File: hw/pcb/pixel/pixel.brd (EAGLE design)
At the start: 160 x 100 mm, 0 parts

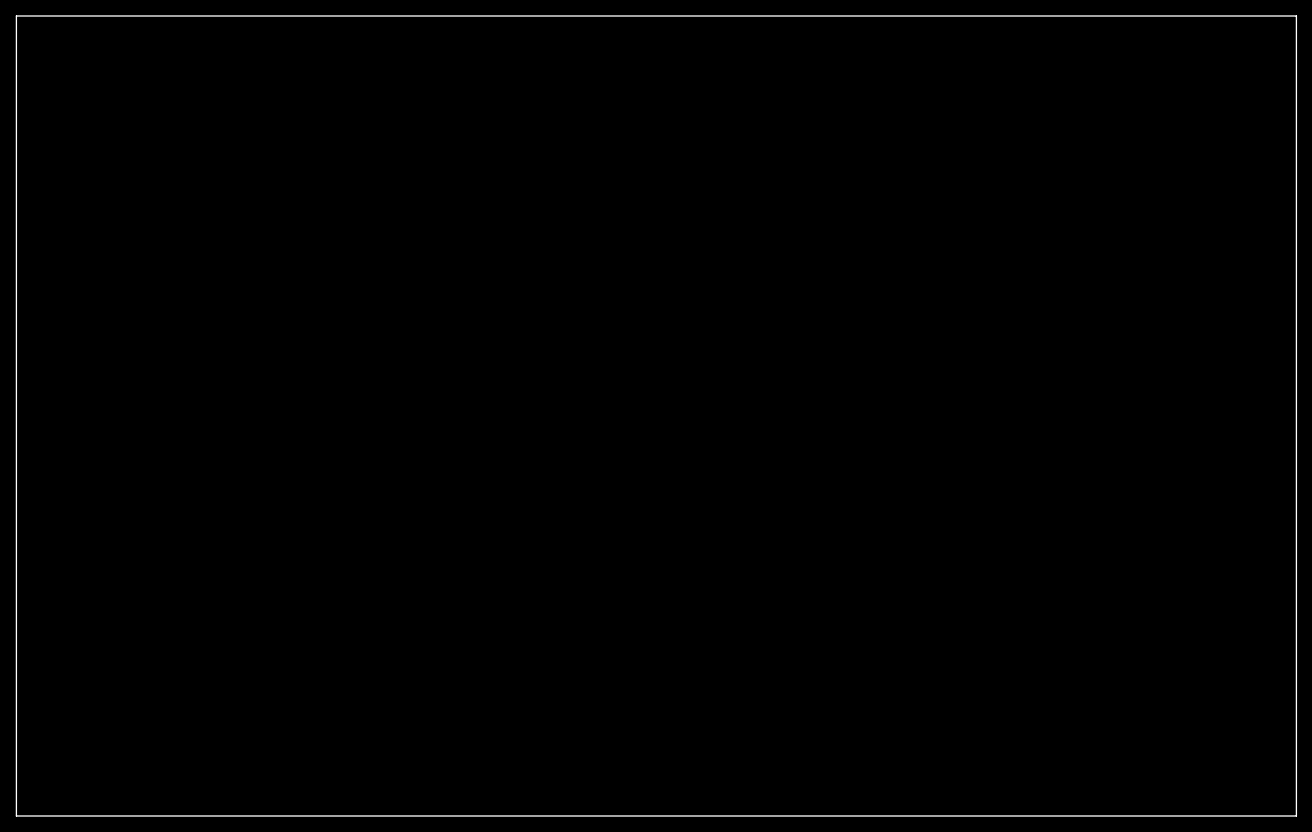
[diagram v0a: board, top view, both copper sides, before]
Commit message: First pass at pixel PCB
- Add some library footprints.
- First pass on schematic and layout of pixel PCB.
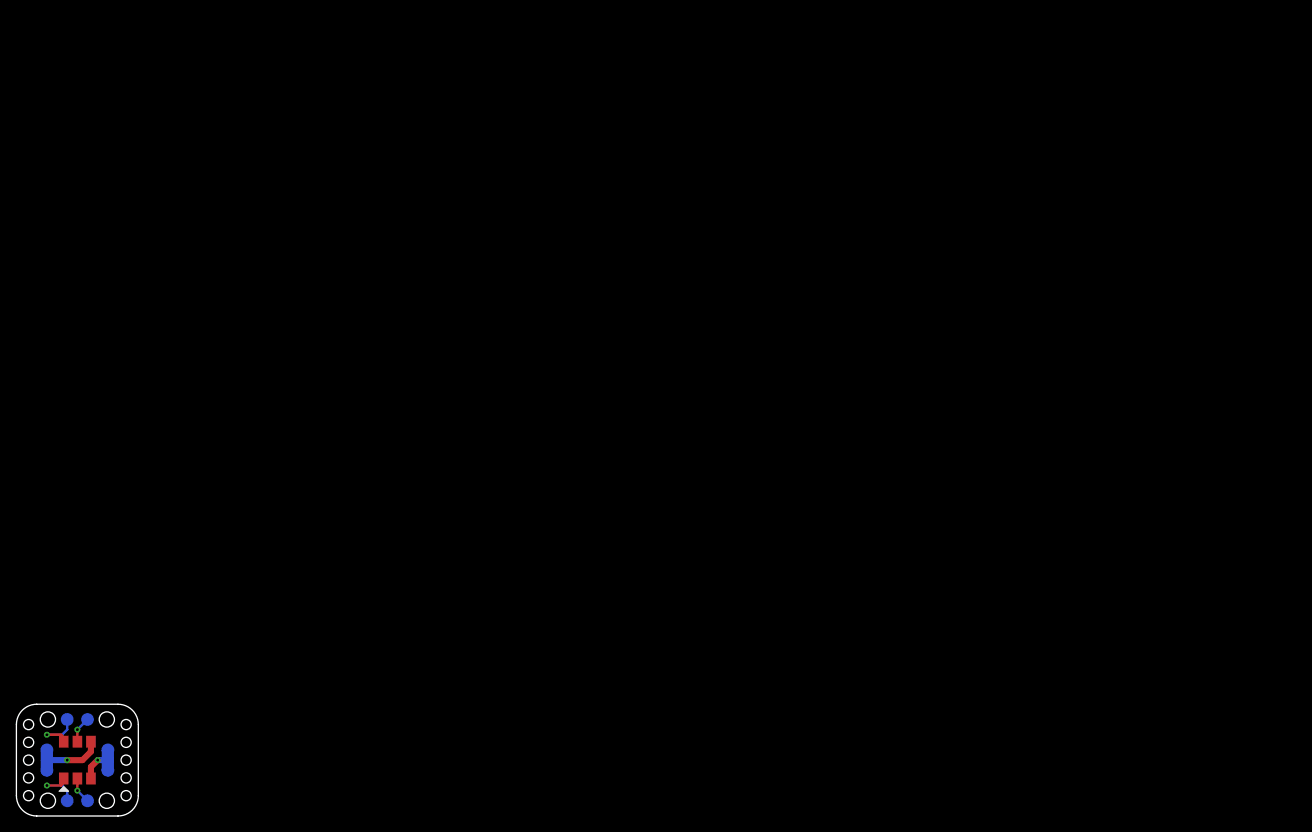
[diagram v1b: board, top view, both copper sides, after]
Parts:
- added TP1, TP2, TP3, TP4, TP5, TP6, TP7, TP8: (no value), wedfestdress:TP_1P6_MM_ROUND
- added U1: (no value), wedfestdress:APA102C
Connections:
- new net CI: TP3.P$1, U1.P2
- new net CO: TP5.P$1, U1.P5
- new net DI: TP2.P$1, U1.P1
- new net DO: TP6.P$1, U1.P6
- new net GND: TP4.P$1, TP8.P$1, U1.P3
- new net V+: TP1.P$1, TP7.P$1, U1.P4
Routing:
- net V+: track 0.00 -> 9.73 mm, vias 0 -> 1
- net DO: track 0.00 -> 6.86 mm, vias 0 -> 1
- net DI: track 0.00 -> 6.86 mm, vias 0 -> 1
- net GND: track 0.00 -> 6.46 mm, vias 0 -> 1
- net CO: track 0.00 -> 3.31 mm, vias 0 -> 1
- net CI: track 0.00 -> 3.31 mm, vias 0 -> 1
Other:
- board size 160 x 100 mm -> 15.2 x 14 mm
- board text added: "C"
- board text added: "D"
- board text added: "V+"
- board text added: "in"
- board text added: "out"

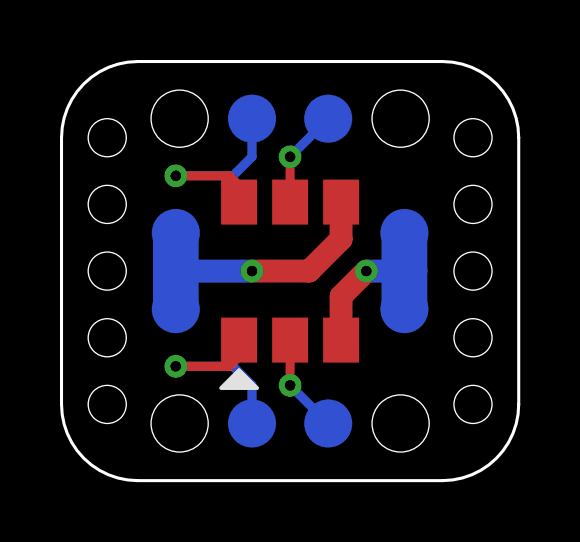
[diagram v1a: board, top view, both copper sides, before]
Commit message: Tweak hole placement and size, tweak design rules
- Added holes for threading power wires twice instead of once.
- Came up with a way to thread the signal wires into the power wired
  so that all are strain relieved well. Two holes on the threading
  holes (small) will be used to thread 28 AWG signal wires through.
  Signal wires will thread through the loop created by the power
  wires.
- Made holes smaller to match candidate wires with OD of 0.4" and
  0.5".
- Moved solder pads on bottom side inward to free up space for more
  strain relief holes.
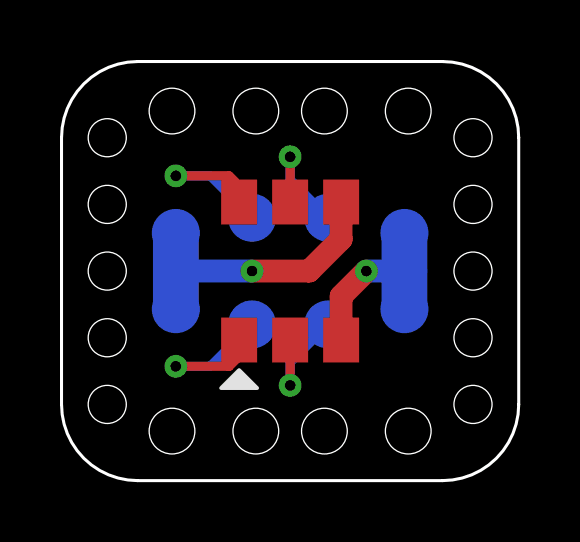
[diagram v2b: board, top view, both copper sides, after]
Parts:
- moved TP2 3.30 mm to (6.35, 5.21)
- moved TP3 3.30 mm to (8.89, 5.21)
- moved TP5 3.30 mm to (8.89, 8.76)
- moved TP6 3.30 mm to (6.35, 8.76)
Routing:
- net DO: track 6.86 -> 5.91 mm
- net DI: track 6.86 -> 5.91 mm
- net CO: track 3.31 -> 4.07 mm
- net CI: track 3.31 -> 4.07 mm

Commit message: Draft of schematic is complete
Still needs review.
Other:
- board text added: "IN"
- board text added: "OUT"
- board text removed: "in"
- board text removed: "out"
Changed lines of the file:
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@@
 <setting verticaltext="up"/>
 </settings>
-<grid distance="0.01" unitdist="inch" unit="inch" style="lines" multiple="1" display="no" altdistance="0.01" altunitdist="inch" altunit="inch"/>
+<grid distance="0.01" unitdist="inch" unit="inch" style="lines" multiple="1" display="no" altdistance="0.0025" altunitdist="inch" altunit="inch"/>
 <layers>
 <layer number="1" name="Top" color="4" fill="1" visible="yes" active="yes"/>
@@
 <hole x="1.524" y="9.2075" drill="1.27"/>
 <hole x="1.524" y="4.7625" drill="1.27"/>
-<text x="4.318" y="3.302" size="1.27" layer="22" rot="MR0">V+</text>
+<text x="4.318" y="3.302" size="1.27" layer="22" font="vector" rot="MR0">V+</text>
 <wire x1="11.43" y1="9.906" x2="11.43" y2="10.668" width="0.2032" layer="22"/>
 <polygon width="0.2032" layer="22">
@@
 <vertex x="11.43" y="9.398"/>
 </polygon>
-<text x="7.62" y="3.048" size="1.27" layer="22" rot="MR0" align="bottom-center">in</text>
-<text x="7.62" y="9.906" size="1.27" layer="22" rot="MR0" align="bottom-center">out</text>
-<text x="5.588" y="10.16" size="0.762" layer="22" rot="MR0">D</text>
-<text x="10.414" y="10.16" size="0.762" layer="22" rot="MR0">C</text>
-<text x="10.414" y="3.048" size="0.762" layer="22" rot="MR0">C</text>
-<text x="5.588" y="3.048" size="0.762" layer="22" rot="MR0">D</text>
+<text x="7.493" y="2.6035" size="1.016" layer="22" font="vector" rot="MR0" align="bottom-center">IN</text>
+<text x="7.62" y="10.287" size="1.016" layer="22" font="vector" rot="MR0" align="bottom-center">OUT</text>
+<text x="5.334" y="9.652" size="0.762" layer="22" font="vector" rot="MR0">D</text>
+<text x="10.16" y="9.652" size="0.762" layer="22" font="vector" rot="MR0">C</text>
+<text x="10.414" y="4.064" size="0.762" layer="22" font="vector" rot="MR0">C</text>
+<text x="5.334" y="4.064" size="0.762" layer="22" font="vector" rot="MR0">D</text>
 <hole x="6.477" y="1.651" drill="1.524"/>
 <hole x="8.763" y="1.651" drill="1.524"/>
@@
 <param name="mvStopFrame" value="1"/>
 <param name="mvCreamFrame" value="0"/>
-<param name="mlMinStopFrame" value="4mil"/>
+<param name="mlMinStopFrame" value="3mil"/>
 <param name="mlMaxStopFrame" value="4mil"/>
 <param name="mlMinCreamFrame" value="0mil"/>

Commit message: Final tweaks and CAM output for all three boards
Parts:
- added TVS1, TVS2, TVS3, TVS4: (no value), wedfestdress:SOD523
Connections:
- net CI: now also TVS1.K
- net CO: now also TVS3.K
- net DI: now also TVS2.K
- net DO: now also TVS4.K
- net GND: now also TVS1.A, TVS2.A, TVS3.A, TVS4.A
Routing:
- net GND: track 6.46 -> 16.3 mm
- net CO: track 4.07 -> 9.88 mm
- net CI: track 4.07 -> 9.01 mm
- net DI: track 5.91 -> 8.12 mm
- net DO: track 5.91 -> 7.50 mm
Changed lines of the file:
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@@
 <attribute name="COST_X500" value="" x="11.43" y="8.255" size="1.778" layer="28" rot="MR0" display="off"/>
+</element>
+<element name="TVS1" library="wedfestdress" package="SOD523" value="" x="11.43" y="5.08" smashed="yes" rot="R270">
+<attribute name="PACKAGE" value="SOD523" x="11.43" y="5.08" size="1.778" layer="27" rot="R270" display="off"/>
+<attribute name="DIST_PART_NO" value="1727-5906-1-ND" x="11.43" y="5.08" size="1.778" layer="27" rot="R270" display="off"/>
+<attribute name="COST_X1" value="0.45" x="11.43" y="5.08" size="1.778" layer="27" rot="R270" display="off"/>
+<attribute name="DISTRIBUTOR" value="Digikey" x="11.43" y="5.08" size="1.778" layer="27" rot="R270" display="off"/>
+<attribute name="DESCRIPTION" value="TVS diode, 5 Vs, 5.8 Vbr, 8 Vcl, 0.95 pF, 8 kV, 200 mW" x="11.43" y="5.08" size="1.778" layer="27" rot="R270" display="off"/>
+<attribute name="DISPLAY" value="5.8 Vbr" x="11.43" y="5.08" size="1.778" layer="27" rot="R270" display="off"/>
+<attribute name="COST_X100" value="0.288" x="11.43" y="5.08" size="1.778" layer="27" rot="R270" display="off"/>
+<attribute name="MFG" value="NXP" x="11.43" y="5.08" size="1.778" layer="27" rot="R270" display="off"/>
+<attribute name="MFG_PART_NO" value="PESD5V0X1UB,135" x="11.43" y="5.08" size="1.778" layer="27" rot="R270" display="off"/>
+<attribute name="NOSTUFF" value="" x="11.43" y="5.08" size="1.778" layer="27" rot="R270" display="off"/>
+<attribute name="COST_X500" value="0.22626" x="11.43" y="5.08" size="1.778" layer="27" rot="R270" display="off"/>
+</element>
+<element name="TVS2" library="wedfestdress" package="SOD523" value="" x="4.064" y="5.588" smashed="yes" rot="R270">
+<attribute name="PACKAGE" value="SOD523" x="4.064" y="5.588" size="1.778" layer="27" rot="R270" display="off"/>
+<attribute name="DIST_PART_NO" value="1727-5906-1-ND" x="4.064" y="5.588" size="1.778" layer="27" rot="R270" display="off"/>
+<attribute name="COST_X1" value="0.45" x="4.064" y="5.588" size="1.778" layer="27" rot="R270" display="off"/>
+<attribute name="DISTRIBUTOR" value="Digikey" x="4.064" y="5.588" size="1.778" layer="27" rot="R270" display="off"/>
+<attribute name="DESCRIPTION" value="TVS diode, 5 Vs, 5.8 Vbr, 8 Vcl, 0.95 pF, 8 kV, 200 mW" x="4.064" y="5.588" size="1.778" layer="27" rot="R270" display="off"/>
+<attribute name="DISPLAY" value="5.8 Vbr" x="4.064" y="5.588" size="1.778" layer="27" rot="R270" display="off"/>
+<attribute name="COST_X100" value="0.288" x="4.064" y="5.588" size="1.778" layer="27" rot="R270" display="off"/>
+<attribute name="MFG" value="NXP" x="4.064" y="5.588" size="1.778" layer="27" rot="R270" display="off"/>
+<attribute name="MFG_PART_NO" value="PESD5V0X1UB,135" x="4.064" y="5.588" size="1.778" layer="27" rot="R270" display="off"/>
+<attribute name="NOSTUFF" value="" x="4.064" y="5.588" size="1.778" layer="27" rot="R270" display="off"/>
+<attribute name="COST_X500" value="0.22626" x="4.064" y="5.588" size="1.778" layer="27" rot="R270" display="off"/>
+</element>
+<element name="TVS3" library="wedfestdress" package="SOD523" value="" x="11.43" y="7.874" smashed="yes" rot="R90">
+<attribute name="PACKAGE" value="SOD523" x="11.43" y="7.874" size="1.778" layer="27" rot="R90" display="off"/>
+<attribute name="DIST_PART_NO" value="1727-5906-1-ND" x="11.43" y="7.874" size="1.778" layer="27" rot="R90" display="off"/>
+<attribute name="COST_X1" value="0.45" x="11.43" y="7.874" size="1.778" layer="27" rot="R90" display="off"/>
+<attribute name="DISTRIBUTOR" value="Digikey" x="11.43" y="7.874" size="1.778" layer="27" rot="R90" display="off"/>
+<attribute name="DESCRIPTION" value="TVS diode, 5 Vs, 5.8 Vbr, 8 Vcl, 0.95 pF, 8 kV, 200 mW" x="11.43" y="7.874" size="1.778" layer="27" rot="R90" display="off"/>
+<attribute name="DISPLAY" value="5.8 Vbr" x="11.43" y="7.874" size="1.778" layer="27" rot="R90" display="off"/>
+<attribute name="COST_X100" value="0.288" x="11.43" y="7.874" size="1.778" layer="27" rot="R90" display="off"/>
+<attribute name="MFG" value="NXP" x="11.43" y="7.874" size="1.778" layer="27" rot="R90" display="off"/>
+<attribute name="MFG_PART_NO" value="PESD5V0X1UB,135" x="11.43" y="7.874" size="1.778" layer="27" rot="R90" display="off"/>
+<attribute name="NOSTUFF" value="" x="11.43" y="7.874" size="1.778" layer="27" rot="R90" display="off"/>
+<attribute name="COST_X500" value="0.22626" x="11.43" y="7.874" size="1.778" layer="27" rot="R90" display="off"/>
+</element>
+<element name="TVS4" library="wedfestdress" package="SOD523" value="" x="4.064" y="8.128" smashed="yes" rot="R90">
+<attribute name="PACKAGE" value="SOD523" x="4.064" y="8.128" size="1.778" layer="27" rot="R90" display="off"/>
+<attribute name="DIST_PART_NO" value="1727-5906-1-ND" x="4.064" y="8.128" size="1.778" layer="27" rot="R90" display="off"/>
+<attribute name="COST_X1" value="0.45" x="4.064" y="8.128" size="1.778" layer="27" rot="R90" display="off"/>
+<attribute name="DISTRIBUTOR" value="Digikey" x="4.064" y="8.128" size="1.778" layer="27" rot="R90" display="off"/>
+<attribute name="DESCRIPTION" value="TVS diode, 5 Vs, 5.8 Vbr, 8 Vcl, 0.95 pF, 8 kV, 200 mW" x="4.064" y="8.128" size="1.778" layer="27" rot="R90" display="off"/>
+<attribute name="DISPLAY" value="5.8 Vbr" x="4.064" y="8.128" size="1.778" layer="27" rot="R90" display="off"/>
+<attribute name="COST_X100" value="0.288" x="4.064" y="8.128" size="1.778" layer="27" rot="R90" display="off"/>
+<attribute name="MFG" value="NXP" x="4.064" y="8.128" size="1.778" layer="27" rot="R90" display="off"/>
+<attribute name="MFG_PART_NO" value="PESD5V0X1UB,135" x="4.064" y="8.128" size="1.778" layer="27" rot="R90" display="off"/>
+<attribute name="NOSTUFF" value="" x="4.064" y="8.128" size="1.778" layer="27" rot="R90" display="off"/>
+<attribute name="COST_X500" value="0.22626" x="4.064" y="8.128" size="1.778" layer="27" rot="R90" display="off"/>
 </element>
 </elements>
@@
 <wire x1="3.81" y1="3.81" x2="4.953" y2="3.81" width="0.3048" layer="16"/>
 <wire x1="4.953" y1="3.81" x2="6.35" y2="5.207" width="0.3048" layer="16"/>
+<contactref element="TVS2" pad="K"/>
+<wire x1="4.064" y1="5.038" x2="5.92" y2="5.038" width="0.4064" layer="1"/>
+<wire x1="5.92" y1="5.038" x2="5.92" y2="4.685" width="0.4064" layer="1"/>
 </signal>
 <signal name="CI">
@@
 <wire x1="7.62" y1="3.175" x2="7.62" y2="3.937" width="0.3048" layer="16"/>
 <wire x1="7.62" y1="3.937" x2="8.89" y2="5.207" width="0.3048" layer="16"/>
+<contactref element="TVS1" pad="K"/>
+<wire x1="11.43" y1="4.53" x2="11.43" y2="3.556" width="0.4064" layer="1"/>
+<wire x1="11.43" y1="3.556" x2="11.049" y2="3.175" width="0.4064" layer="1"/>
+<wire x1="11.049" y1="3.175" x2="7.62" y2="3.175" width="0.4064" layer="1"/>
 </signal>
 <signal name="DO">
@@
 <wire x1="3.81" y1="10.16" x2="4.953" y2="10.16" width="0.3048" layer="16"/>
 <wire x1="4.953" y1="10.16" x2="6.35" y2="8.763" width="0.3048" layer="16"/>
+<contactref element="TVS4" pad="K"/>
+<wire x1="4.064" y1="8.678" x2="4.064" y2="9.398" width="0.4064" layer="1"/>
+<wire x1="4.064" y1="9.398" x2="3.81" y2="9.652" width="0.4064" layer="1"/>
+<wire x1="3.81" y1="9.652" x2="3.81" y2="10.16" width="0.4064" layer="1"/>
 </signal>
 <signal name="CO">
@@
 <wire x1="7.62" y1="10.795" x2="7.62" y2="10.033" width="0.3048" layer="16"/>
 <wire x1="7.62" y1="10.033" x2="8.89" y2="8.763" width="0.3048" layer="16"/>
+<contactref element="TVS3" pad="K"/>
+<wire x1="11.43" y1="8.424" x2="11.43" y2="10.16" width="0.4064" layer="1"/>
+<wire x1="11.43" y1="10.16" x2="10.795" y2="10.795" width="0.4064" layer="1"/>
+<wire x1="10.795" y1="10.795" x2="7.62" y2="10.795" width="0.4064" layer="1"/>
 </signal>
 <signal name="GND">
@@
 <wire x1="11.43" y1="6.985" x2="11.43" y2="8.255" width="1.524" layer="16"/>
 <wire x1="11.43" y1="5.715" x2="11.43" y2="6.985" width="1.524" layer="16"/>
+<contactref element="TVS2" pad="A"/>
+<contactref element="TVS1" pad="A"/>
+<contactref element="TVS4" pad="A"/>
+<contactref element="TVS3" pad="A"/>
+<wire x1="4.064" y1="6.138" x2="9.32" y2="6.138" width="0.4064" layer="1"/>
+<wire x1="9.32" y1="6.138" x2="9.32" y2="6.145" width="0.4064" layer="1"/>
+<wire x1="4.064" y1="6.138" x2="4.064" y2="7.578" width="0.4064" layer="1"/>
+<wire x1="11.43" y1="5.63" x2="11.43" y2="7.324" width="0.4064" layer="1"/>
+<wire x1="10.16" y1="6.985" x2="10.499" y2="7.324" width="0.4064" layer="1"/>
+<wire x1="10.499" y1="7.324" x2="11.43" y2="7.324" width="0.4064" layer="1"/>
 </signal>
 </signals>
